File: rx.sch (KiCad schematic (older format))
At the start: 20 parts, among them T1 Transformer_1P_SS, U3 SN74CBT3253, U9 LT6231CSB

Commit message: Added RF front end and LNA
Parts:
- added C? (x13): 100n, Capacitor_SMD:C_0603_1608Metric, symbol DeltaSDR-rescue:C-Device-DeltaSDR-rescue
- added C? (x2): 5n6, Capacitor_SMD:C_0603_1608Metric, symbol DeltaSDR-rescue:C-Device-DeltaSDR-rescue
- added C? (x4): 1800p, Capacitor_SMD:C_0603_1608Metric, symbol DeltaSDR-rescue:C-Device-DeltaSDR-rescue
- added C? (x2): 270p, Capacitor_SMD:C_0603_1608Metric, symbol DeltaSDR-rescue:C-Device-DeltaSDR-rescue
- added D? (x4): BAP64-06, symbol Device:D_x2_ACom_KKA
- added J?: Conn_Coaxial, symbol Connector:Conn_Coaxial
- added L? (x5): 15u, symbol Device:L
- added L?: 390n, symbol Device:L
- added L? (x4): 1u, symbol Device:L
- added L? (x2): 6u8, symbol Device:L
- added Q? (x6): BSS123, Package_TO_SOT_SMD:SOT-23, symbol Transistor_FET:BSS123
- added R? (x9): 2k2, Resistor_SMD:R_0603_1608Metric, symbol DeltaSDR-rescue:R-Device-DeltaSDR-rescue
- added R? (x6): 100k, Resistor_SMD:R_0603_1608Metric, symbol DeltaSDR-rescue:R-Device-DeltaSDR-rescue
- added R? (x2): 27R, Resistor_SMD:R_0603_1608Metric, symbol DeltaSDR-rescue:R-Device-DeltaSDR-rescue
- added R?: 270R, Resistor_SMD:R_0603_1608Metric, symbol DeltaSDR-rescue:R-Device-DeltaSDR-rescue
- added U?: MMG3H21NT1, Package_TO_SOT_SMD:SOT-89-3, symbol RF_Amplifier:SPF5189Z
- C25, C26, C27, C28, C29, C30, C31, C32, C33: symbol DeltaSDR-rescue:C-Device -> DeltaSDR-rescue:C-Device-DeltaSDR-rescue
- R10, R11, R12, R13, R14, R15, R16, R9: symbol DeltaSDR-rescue:R-Device -> DeltaSDR-rescue:R-Device-DeltaSDR-rescue
- T1: symbol DeltaSDR-rescue:Transformer_1P_SS-Device -> DeltaSDR-rescue:Transformer_1P_SS-Device-DeltaSDR-rescue
- U3: symbol DeltaSDR-rescue:SN74CBT3253-Analog_Switch -> DeltaSDR-rescue:SN74CBT3253-Analog_Switch-DeltaSDR-rescue
- U9: symbol DeltaSDR-rescue:Opamp_Dual_Generic-Device -> DeltaSDR-rescue:Opamp_Dual_Generic-Device-DeltaSDR-rescue
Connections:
- net labels added: +12V, B6040M, B80M, HI_RX, HI_TX, PA_IN, RF_BIT, RX_RF, TX_OUT
- wire segments 99 -> 274
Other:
- note added: "40/60M\n"
- note added: "80M\n"

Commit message: First layouting
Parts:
- C32: footprint Capacitor_SMD:C_0603_1608Metric -> Capacitor_SMD:C_0805_2012Metric
- C57, C63: renamed from C?; value 1800p -> 1n
- C61: renamed from C?; value 270p -> 200p
- D4, D5, D6, D7: renamed from D?; footprint (none) -> Package_TO_SOT_SMD:SOT-23
- J5: renamed from J?; footprint (none) -> Connector_Coaxial:SMA_Amphenol_132289_EdgeMount
- L10, L11, L13, L2, L3: renamed from L?; footprint (none) -> Inductor_SMD:L_Taiyo-Yuden_NR-30xx_HandSoldering
- L12: renamed from L?; footprint (none) -> Inductor_SMD:L_0805_2012Metric
- L4, L8: renamed from L?; value 1u -> 680n; footprint (none) -> Inductor_SMD:L_Abracon_ASPI-3012S
- L5, L7, L9: renamed from L?; footprint (none) -> Inductor_SMD:L_Abracon_ASPI-3012S
- L6: renamed from L?; value 6u8 -> 3u3; footprint (none) -> Inductor_SMD:L_Abracon_ASPI-3012S
- T1: footprint (none) -> Transformer_SMD:Transformer_MACOM_SM-22
- U9: footprint (none) -> Package_SO:SO-8_3.9x4.9mm_P1.27mm
- gave numbers to parts that had none: 43
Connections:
- net QSE_J renamed QSD_J
- net QSE_Q renamed QSD_Q

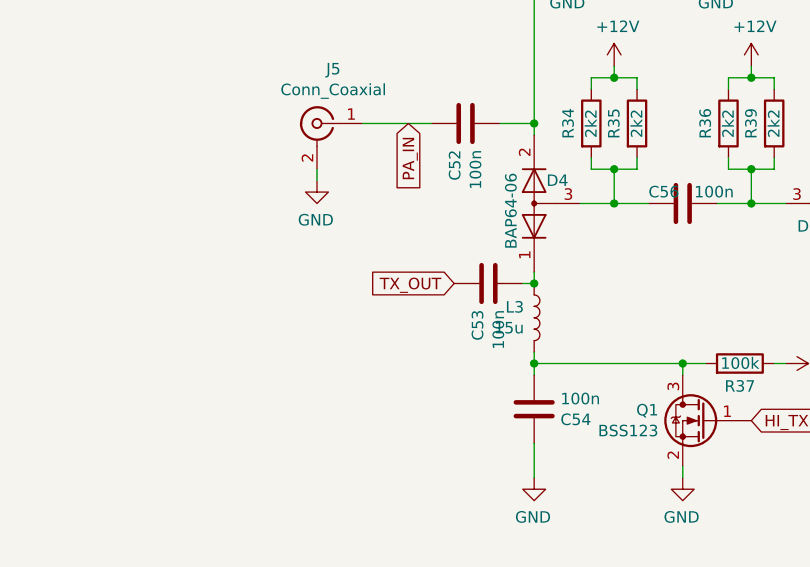
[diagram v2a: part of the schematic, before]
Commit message: Layout: All components connected
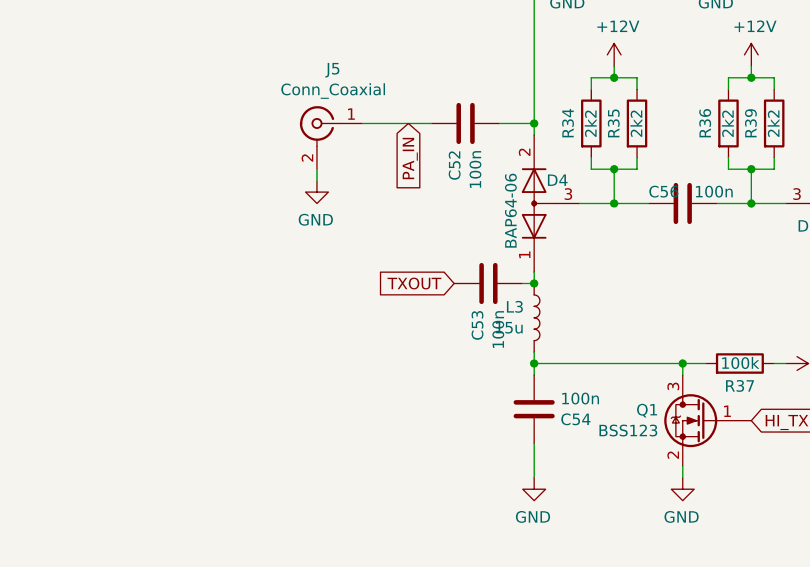
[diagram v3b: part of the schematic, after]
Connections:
- net TX_OUT renamed TXOUT
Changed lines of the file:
@@
 $EndComp
 Text GLabel 3900 3350 0    50   Input ~ 0
-TX_OUT
+TXOUT
 $Comp
 L Device:L L?

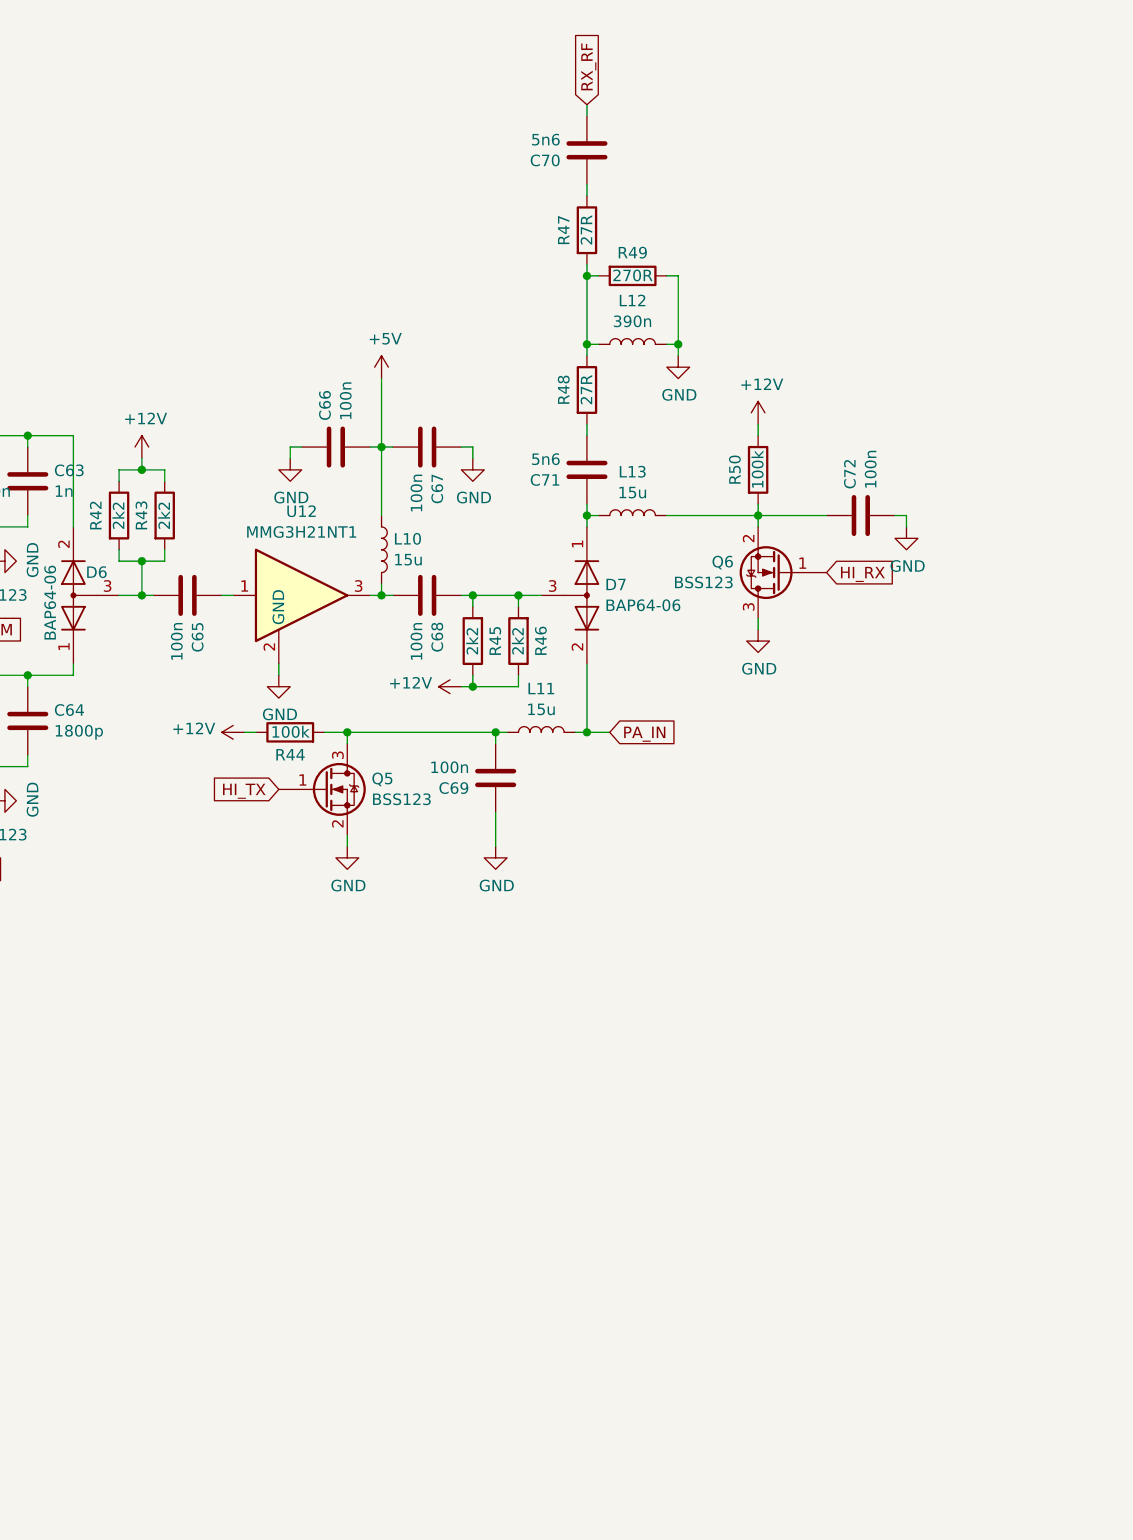
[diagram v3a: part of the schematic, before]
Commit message: Changed board size, changed PA_IN signal position, changed LDOs, added 50 ohm tracks andvias
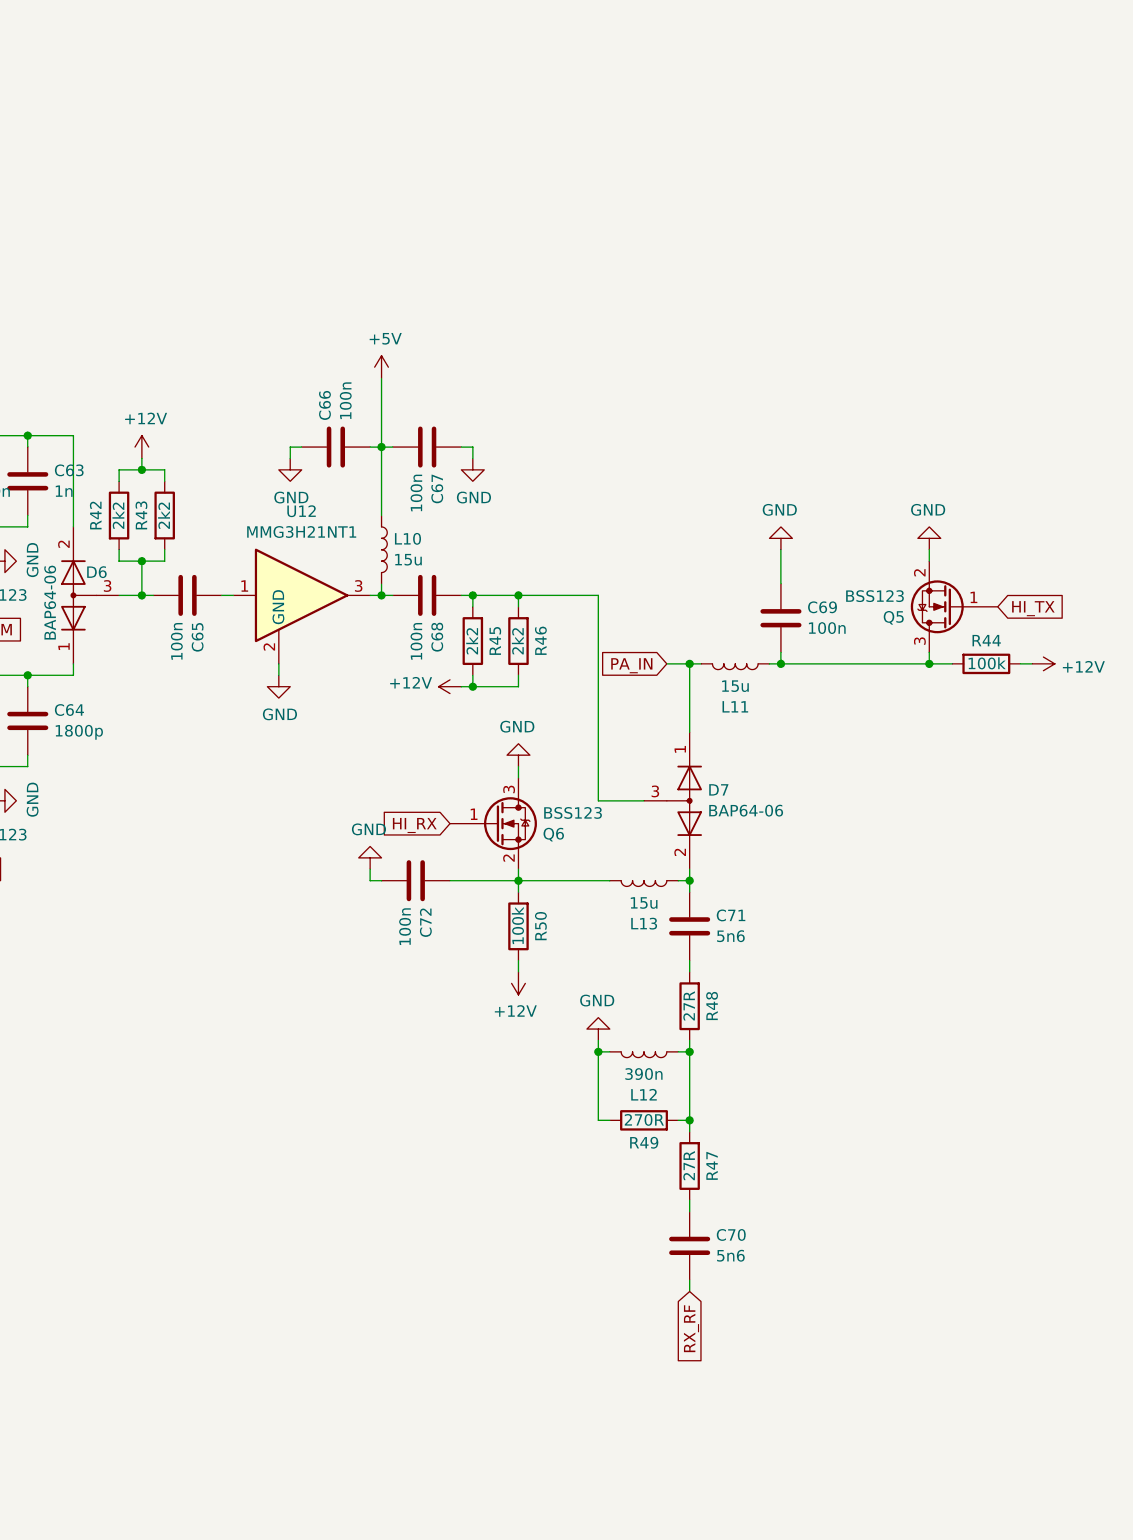
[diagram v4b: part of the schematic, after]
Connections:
- net PA_IN: now also D7.1 (K); no longer D7.2 (K)
- net at C71.1, L13.1: now also D7.2 (K); no longer D7.1 (K)
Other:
- moved on the sheet: C69, C70, C71, C72, D7, L11, L12, L13, Q5, Q6, R44, R47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

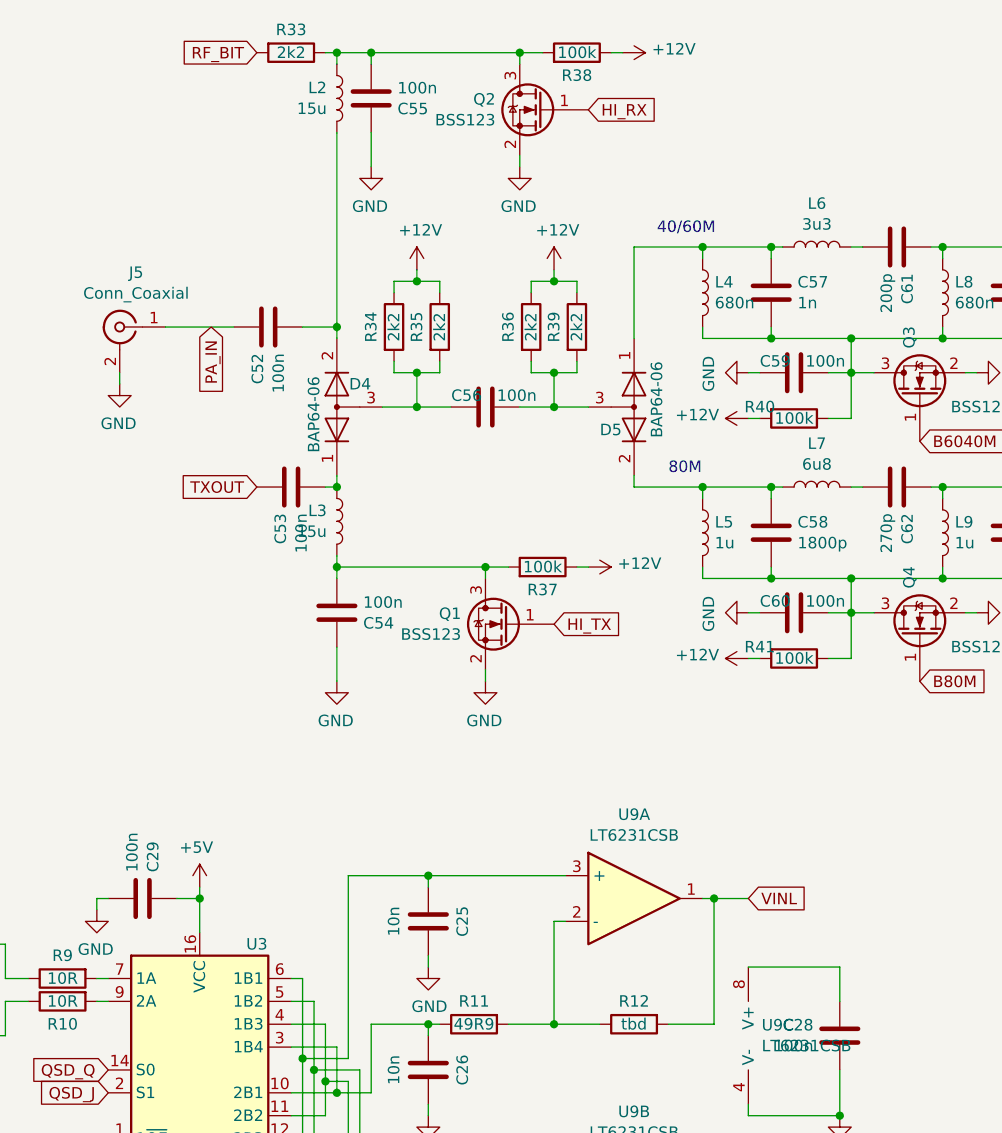
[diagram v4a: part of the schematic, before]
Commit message: ERC, DRC done, added output for ATU and AMP
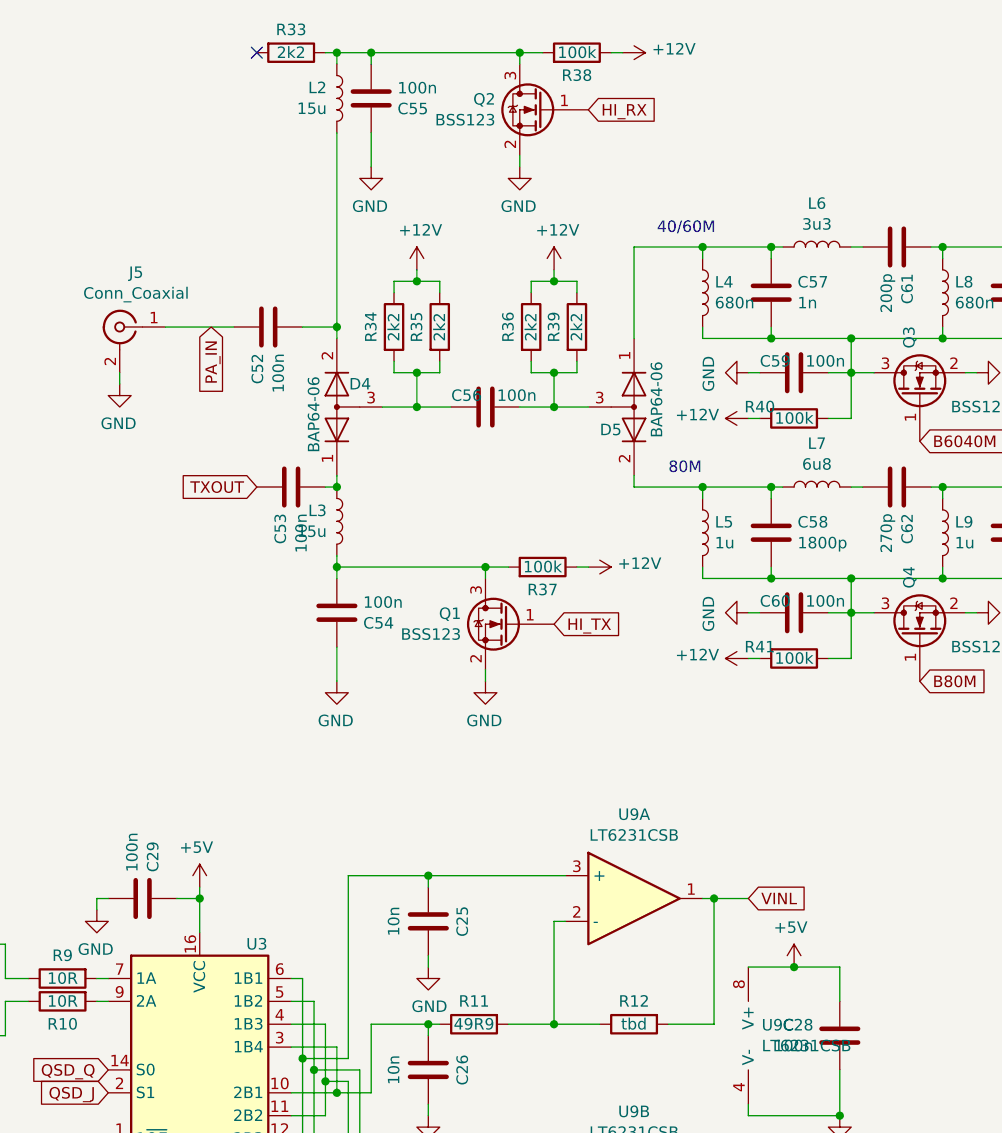
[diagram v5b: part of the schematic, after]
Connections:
- net +5V: now also C28.1, U9.8 (V+)
- net RF_BIT: no longer names the net of R33.2
- no-connect marks 0 -> 1
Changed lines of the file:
@@
 Connection ~ 6450 6100
 Wire Wire Line
-	6050 5450 6450 5450
+	6050 5450 6250 5450
 Wire Wire Line
 	6450 5450 6450 5600
@@
 HI_RX
 Connection ~ 4400 1450
-Text GLabel 3900 1450 0    50   Input ~ 0
-RF_BIT
 $Comp
 L DeltaSDR-rescue:R-Device-DeltaSDR-rescue R?
@@
 Wire Wire Line
 	9350 3000 9700 3000
+$Comp
+L power:+5V #PWR0228
+U 1 1 5EA9AC2A
+P 6250 5450
+F 0 "#PWR0228" H 6250 5300 50  0001 C CNN
+F 1 "+5V" H 6265 5623 50  0000 C CNN
+F 2 "" H 6250 5450 50  0001 C CNN
+F 3 "" H 6250 5450 50  0001 C CNN
+	1    6250 5450
+	-1   0    0    -1
+$EndComp
+Connection ~ 6250 5450
+Wire Wire Line
+	6250 5450 6450 5450
+NoConn ~ 3900 1450
 $EndSCHEMATC

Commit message: Corrected Q6 connection, RX schematic clean up
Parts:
- removed R33: 2k2, Resistor_SMD:R_0603_1608Metric, symbol DeltaSDR-rescue:R-Device-DeltaSDR-rescue
- D4, D5, D6, D7: symbol Device:D_x2_ACom_KKA -> DeltaSDR-rescue:D_x2_ACom_KKA-Device
- J5: symbol Connector:Conn_Coaxial -> DeltaSDR-rescue:Conn_Coaxial-Connector
- L10, L11, L12, L13, L2, L3, L4, L5, L6, L7, L8, L9: symbol Device:L -> DeltaSDR-rescue:L-Device
- Q1, Q2, Q3, Q4, Q5, Q6: symbol Transistor_FET:BSS123 -> DeltaSDR-rescue:BSS123-Transistor_FET
- U12: symbol RF_Amplifier:SPF5189Z -> DeltaSDR-rescue:SPF5189Z-RF_Amplifier
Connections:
- net +12V: now also R44.2; no longer R44.1
- net GND: now also Q6.2 (S); no longer Q6.3 (D)
- net at C69.2, L11.1, Q5.3 (D): now also R44.1; no longer R44.2
- net at C72.1, L13.2, R50.2: now also Q6.3 (D); no longer Q6.2 (S)
- no-connect marks 1 -> 0
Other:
- moved on the sheet: C52, C53, C54, C55, C56, C57, C58, C59, C60, C61, C62, C63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

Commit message: Changed mixers footprints, added 3D models, silk screen correction
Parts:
- U3: footprint Package_SO:SOIC-16_4.55x10.3mm_P1.27mm -> Package_SO:SOIC-16_3.9x9.9mm_P1.27mm
- U9: footprint Package_SO:SO-8_3.9x4.9mm_P1.27mm -> Package_SO:SOIC-8_3.9x4.9mm_P1.27mm
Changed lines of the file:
@@
 F 0 "U3" H 3900 6450 50  0000 C CNN
 F 1 "SN74CBT3253" H 3950 5300 50  0000 C CNN
-F 2 "Package_SO:SOIC-16_4.55x10.3mm_P1.27mm" H 3650 5900 50  0001 C CNN
+F 2 "Package_SO:SOIC-16_3.9x9.9mm_P1.27mm" H 3650 5900 50  0001 C CNN
 F 3 "http://www.ti.com/lit/gpn/sn74cbt3253" H 3650 5900 50  0001 C CNN
 	1    3650 5900
@@
 F 0 "U9" V 5975 5675 50  0000 L CNN
 F 1 "LT6231CSB" V 6125 5525 50  0000 L CNN
-F 2 "Package_SO:SO-8_3.9x4.9mm_P1.27mm" H 6150 5750 50  0001 C CNN
+F 2 "Package_SO:SOIC-8_3.9x4.9mm_P1.27mm" H 6150 5750 50  0001 C CNN
 F 3 "~" H 6150 5750 50  0001 C CNN
 	3    6150 5750
@@
 F 0 "U9" H 5550 6817 50  0000 C CNN
 F 1 "LT6231CSB" H 5550 6726 50  0000 C CNN
-F 2 "Package_SO:SO-8_3.9x4.9mm_P1.27mm" H 5550 6450 50  0001 C CNN
+F 2 "Package_SO:SOIC-8_3.9x4.9mm_P1.27mm" H 5550 6450 50  0001 C CNN
 F 3 "~" H 5550 6450 50  0001 C CNN
 	2    5550 6450
@@
 F 0 "U9" H 5550 5517 50  0000 C CNN
 F 1 "LT6231CSB" H 5550 5426 50  0000 C CNN
-F 2 "Package_SO:SO-8_3.9x4.9mm_P1.27mm" H 5550 5150 50  0001 C CNN
+F 2 "Package_SO:SOIC-8_3.9x4.9mm_P1.27mm" H 5550 5150 50  0001 C CNN
 F 3 "~" H 5550 5150 50  0001 C CNN
 	1    5550 5150

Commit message: Changed layout of LT6231, changed RX transformer caps ground.
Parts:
- C25, C26, C27, C33: footprint Capacitor_SMD:C_0805_2012Metric -> Capacitor_SMD:C_0603_1608Metric
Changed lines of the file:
@@
 EESchema Schematic File Version 4
-EELAYER 30 0
+LIBS:DeltaSDR-cache
+EELAYER 29 0
 EELAYER END
 $Descr A4 11693 8268
@@
 F 0 "C25" V 4500 5250 50  0000 C CNN
 F 1 "10n" V 4800 5250 50  0000 C CNN
-F 2 "Capacitor_SMD:C_0805_2012Metric" H 4688 5100 50  0001 C CNN
+F 2 "Capacitor_SMD:C_0603_1608Metric" H 4688 5100 50  0001 C CNN
 F 3 "~" H 4650 5250 50  0001 C CNN
 	1    4650 5250
@@
 F 0 "C26" V 4500 5900 50  0000 C CNN
 F 1 "10n" V 4800 5900 50  0000 C CNN
-F 2 "Capacitor_SMD:C_0805_2012Metric" H 4688 5750 50  0001 C CNN
+F 2 "Capacitor_SMD:C_0603_1608Metric" H 4688 5750 50  0001 C CNN
 F 3 "~" H 4650 5900 50  0001 C CNN
 	1    4650 5900
@@
 F 0 "C27" V 4500 6550 50  0000 C CNN
 F 1 "10n" V 4800 6550 50  0000 C CNN
-F 2 "Capacitor_SMD:C_0805_2012Metric" H 4688 6400 50  0001 C CNN
+F 2 "Capacitor_SMD:C_0603_1608Metric" H 4688 6400 50  0001 C CNN
 F 3 "~" H 4650 6550 50  0001 C CNN
 	1    4650 6550
@@
 F 0 "C33" V 4500 7200 50  0000 C CNN
 F 1 "10n" V 4800 7200 50  0000 C CNN
-F 2 "Capacitor_SMD:C_0805_2012Metric" H 4688 7050 50  0001 C CNN
+F 2 "Capacitor_SMD:C_0603_1608Metric" H 4688 7050 50  0001 C CNN
 F 3 "~" H 4650 7200 50  0001 C CNN
 	1    4650 7200
